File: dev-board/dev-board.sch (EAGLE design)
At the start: 37 parts, among them J1 12401832E402A, U1 STM32F103RET6, U2 AT24C64BN-10SU-2.7, U3 FT232RL, U4 MCP2551, U5 LM1117IMP-3.3, X1 8MHz

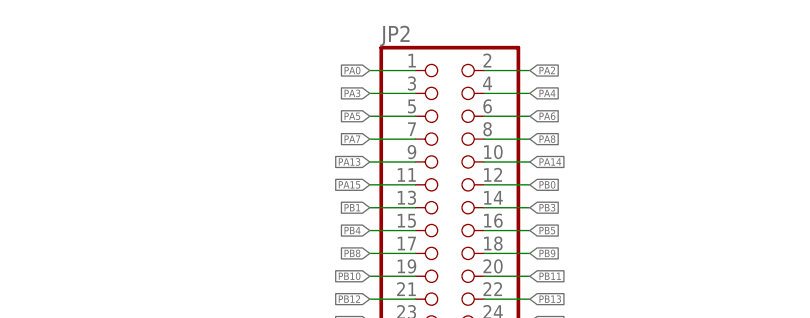
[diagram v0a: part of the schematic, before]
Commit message: Fix dev-board silkscreen
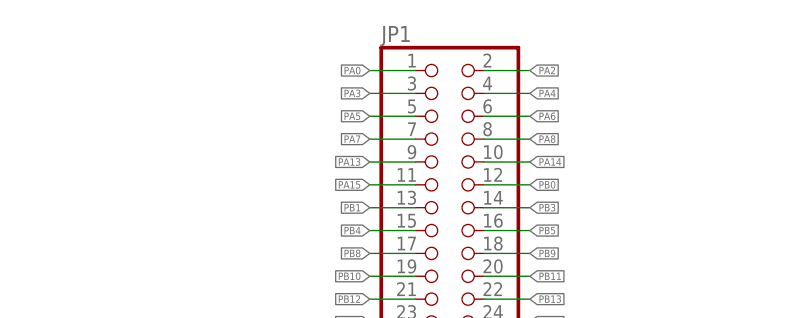
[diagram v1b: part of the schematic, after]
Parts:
- renumbered JP2 to JP1

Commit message: Fix some issues with the dev-board design
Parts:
- added JP2: PINHD-2X20, Connector:PINHD-2X20
- JP1: value PINHD-2X20 -> PINHD-1X4; device Connector:PINHD-2X20 -> Connector:PINHD-1X4
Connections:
- removed net PA13: JP1.9, U1A.PA13
- removed net PA14: JP1.10, U1A.PA14
- new net SWCLK: JP1.3, JP2.10, U1A.PA14
- new net SWDIO: JP1.2, JP2.9, U1A.PA13
- net +5V: now also JP1.1
- net GND: now also JP1.4
- net PA0: now also JP2.1; no longer JP1.1
- net PA15: now also JP2.11; no longer JP1.11
- net PA2: now also JP2.2; no longer JP1.2
- net PA3: now also JP2.3; no longer JP1.3
- net PA4: now also JP2.4; no longer JP1.4
- net PA5: now also JP2.5; no longer JP1.5
- net PA6: now also JP2.6; no longer JP1.6
- net PA7: now also JP2.7; no longer JP1.7
- net PA8: now also JP2.8; no longer JP1.8
- net PB0: now also JP2.12; no longer JP1.12
- net PB1: now also JP2.13; no longer JP1.13
- net PB10: now also JP2.19; no longer JP1.19
- net PB11: now also JP2.20; no longer JP1.20
- net PB12: now also JP2.21; no longer JP1.21
- net PB13: now also JP2.22; no longer JP1.22
- net PB14: now also JP2.23; no longer JP1.23
- net PB15: now also JP2.24; no longer JP1.24
- net PB3: now also JP2.14; no longer JP1.14
- net PB4: now also JP2.15; no longer JP1.15
- net PB5: now also JP2.16; no longer JP1.16
- net PB8: now also JP2.17; no longer JP1.17
- net PB9: now also JP2.18; no longer JP1.18
- net PC0: now also JP2.25; no longer JP1.25
- net PC1: now also JP2.26; no longer JP1.26
- net PC10: now also JP2.35; no longer JP1.35
- net PC11: now also JP2.36; no longer JP1.36
- net PC12: now also JP2.37; no longer JP1.37
- net PC13: now also JP2.38; no longer JP1.38
- net PC14: now also JP2.39; no longer JP1.39
- net PC15: now also JP2.40; no longer JP1.40
- net PC2: now also JP2.27; no longer JP1.27
- net PC3: now also JP2.28; no longer JP1.28
- net PC4: now also JP2.29; no longer JP1.29
- net PC5: now also JP2.30; no longer JP1.30
- net PC6: now also JP2.31; no longer JP1.31
- net PC7: now also JP2.32; no longer JP1.32
- net PC8: now also JP2.33; no longer JP1.33
- net PC9: now also JP2.34; no longer JP1.34

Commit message: Clean up dev-board schematic
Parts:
- R1, R11, R13, R14, R2, R3, R4, R7, R8: value 6K8 -> 10K
- R5, R6: value 6K8 -> 4k7
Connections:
- net N$14 renamed USBDP
- net N$16 renamed USBDM
- net N$7 renamed CANH
- net N$8 renamed CANL
- net +3V3: now also C3.1, U5.OUT_2; no longer C3.2
- net GND: now also C3.2, J1.SHIELD1, J1.SHIELD2, J1.SHIELD3, J1.SHIELD4; no longer C3.1
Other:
- moved on the sheet: C1, C10, C11, C12, C2, C3, C6, C7, J1, J2, R1, R10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

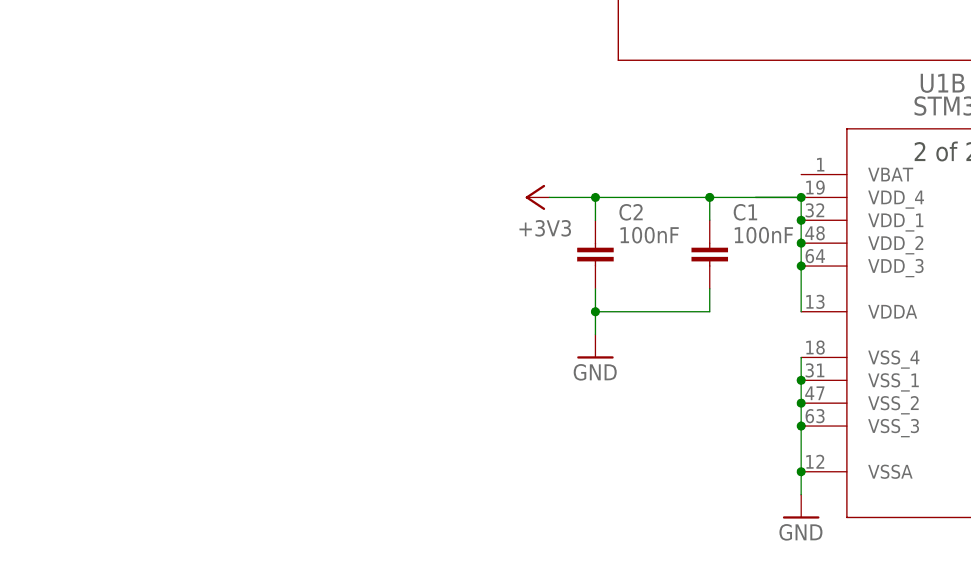
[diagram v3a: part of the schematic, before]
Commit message: Proper decoupling caps for stm32
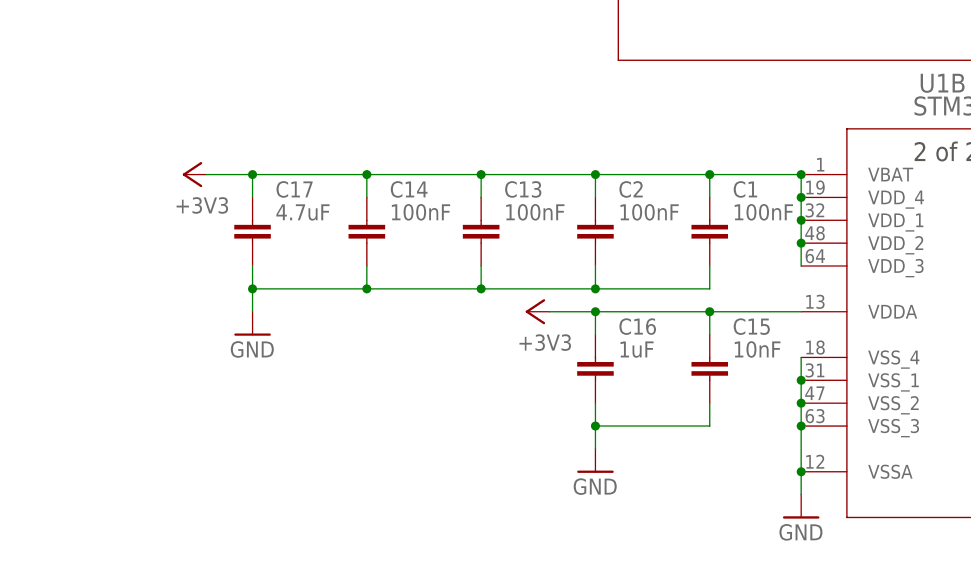
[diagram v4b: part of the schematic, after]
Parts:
- added C13, C14: 100nF, Capacitor:C_CHIP-0805(2012-METRIC)
- added C15: 10nF, Capacitor:C_CHIP-0805(2012-METRIC)
- added C16: 1uF, Capacitor:C_CHIP-0805(2012-METRIC)
- added C17: 4.7uF, Capacitor:C_CHIP-0805(2012-METRIC)
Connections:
- net +3V3: now also C13.1, C14.1, C15.1, C16.1, C17.1, U1B.VBAT
- net GND: now also C13.2, C14.2, C15.2, C16.2, C17.2
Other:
- moved on the sheet: C1, C2

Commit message: Proper bulk cap for regulator
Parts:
- C12: value 100nF -> 10uF
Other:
- moved on the sheet: C10, C11, C12, C3, C6, C7, C8, C9, J1, J2, R1, R10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

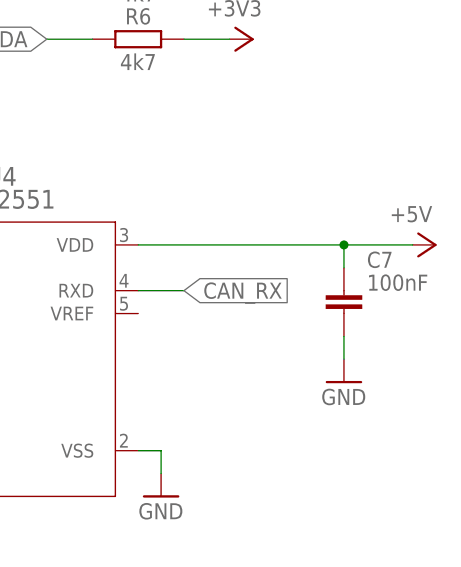
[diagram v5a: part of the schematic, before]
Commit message: Bulkier MCP2551 decoupling cap
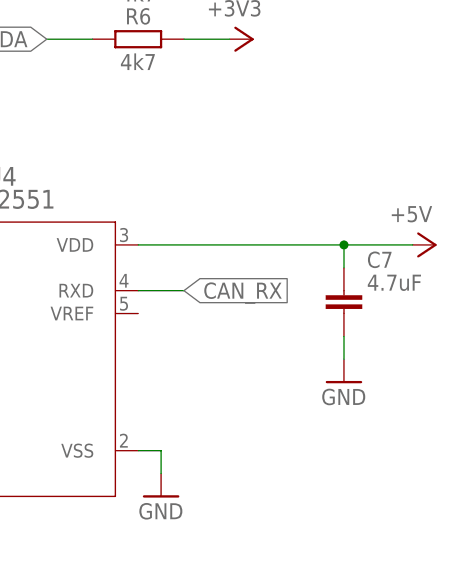
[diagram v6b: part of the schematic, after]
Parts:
- C7: value 100nF -> 4.7uF
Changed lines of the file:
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@@
 <part name="U4" library="IC_Interface" library_urn="urn:adsk.eagle:library:16378299" deviceset="MCP2551" device="_SOIC" package3d_urn="urn:adsk.eagle:package:16378326/2" value="MCP2551"/>
 <part name="GND11" library="supply1" library_urn="urn:adsk.eagle:library:371" deviceset="GND" device=""/>
-<part name="C7" library="Capacitor" library_urn="urn:adsk.eagle:library:16290819" deviceset="C" device="CHIP-0805(2012-METRIC)" package3d_urn="urn:adsk.eagle:package:16290897/2" technology="_" value="100nF"/>
+<part name="C7" library="Capacitor" library_urn="urn:adsk.eagle:library:16290819" deviceset="C" device="CHIP-0805(2012-METRIC)" package3d_urn="urn:adsk.eagle:package:16290897/2" technology="_" value="4.7uF"/>
 <part name="P+4" library="supply1" library_urn="urn:adsk.eagle:library:371" deviceset="+5V" device=""/>
 <part name="C8" library="Capacitor" library_urn="urn:adsk.eagle:library:16290819" deviceset="C" device="CHIP-0805(2012-METRIC)" package3d_urn="urn:adsk.eagle:package:16290897/2" technology="_" value="100nF"/>

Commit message: Fix stm32 decoupling caps in dev-board pcb design
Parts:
- added C18: 100nF, Capacitor:C_CHIP-0805(2012-METRIC)
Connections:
- net +3V3: now also C18.1
- net GND: now also C18.2
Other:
- moved on the sheet: C17
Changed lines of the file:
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@@
 <part name="GND28" library="supply1" library_urn="urn:adsk.eagle:library:371" deviceset="GND" device=""/>
 <part name="GND12" library="supply1" library_urn="urn:adsk.eagle:library:371" deviceset="GND" device=""/>
+<part name="C18" library="Capacitor" library_urn="urn:adsk.eagle:library:16290819" deviceset="C" device="CHIP-0805(2012-METRIC)" package3d_urn="urn:adsk.eagle:package:16290897/2" technology="_" value="100nF"/>
 </parts>
 <sheets>
@@
 <attribute name="VALUE" x="7.3406" y="-54.3814" size="2.0828" layer="96" ratio="6" rot="SR0"/>
 </instance>
-<instance part="+3V1" gate="G$1" x="-73.66" y="-60.96" smashed="yes" rot="R90">
-<attribute name="VALUE" x="-68.58" y="-63.5" size="1.778" layer="96" rot="R180"/>
+<instance part="+3V1" gate="G$1" x="-86.36" y="-60.96" smashed="yes" rot="R90">
+<attribute name="VALUE" x="-81.28" y="-63.5" size="1.778" layer="96" rot="R180"/>
 </instance>
 <instance part="C1" gate="G$1" x="-15.24" y="-66.04" smashed="yes">
@@
 <attribute name="VALUE" x="-30.48" y="-78.74" size="1.778" layer="96" rot="R180"/>
 </instance>
-<instance part="C17" gate="G$1" x="-66.04" y="-66.04" smashed="yes">
+<instance part="C17" gate="G$1" x="-78.74" y="-66.04" smashed="yes">
+<attribute name="NAME" x="-76.2" y="-63.5" size="1.778" layer="95"/>
+<attribute name="VALUE" x="-76.2" y="-66.04" size="1.778" layer="96"/>
+</instance>
+<instance part="GND28" gate="1" x="-78.74" y="-78.74" smashed="yes">
+<attribute name="VALUE" x="-81.28" y="-81.28" size="1.778" layer="96"/>
+</instance>
+<instance part="GND12" gate="1" x="86.36" y="-27.94" smashed="yes">
+<attribute name="VALUE" x="83.82" y="-30.48" size="1.778" layer="96"/>
+</instance>
+<instance part="C18" gate="G$1" x="-66.04" y="-66.04" smashed="yes">
 <attribute name="NAME" x="-63.5" y="-63.5" size="1.778" layer="95"/>
 <attribute name="VALUE" x="-63.5" y="-66.04" size="1.778" layer="96"/>
-</instance>
-<instance part="GND28" gate="1" x="-66.04" y="-78.74" smashed="yes">
-<attribute name="VALUE" x="-68.58" y="-81.28" size="1.778" layer="96"/>
-</instance>
-<instance part="GND12" gate="1" x="86.36" y="-27.94" smashed="yes">
-<attribute name="VALUE" x="83.82" y="-30.48" size="1.778" layer="96"/>
 </instance>
 </instances>
@@
 <wire x1="-15.24" y1="-63.5" x2="-15.24" y2="-60.96" width="0.1524" layer="91"/>
 <pinref part="+3V1" gate="G$1" pin="+3V3"/>
-<wire x1="-71.12" y1="-60.96" x2="-66.04" y2="-60.96" width="0.1524" layer="91"/>
+<wire x1="-83.82" y1="-60.96" x2="-78.74" y2="-60.96" width="0.1524" layer="91"/>
 <junction x="-27.94" y="-60.96"/>
 <pinref part="C14" gate="G$1" pin="1"/>
+<wire x1="-78.74" y1="-60.96" x2="-66.04" y2="-60.96" width="0.1524" layer="91"/>
 <wire x1="-66.04" y1="-60.96" x2="-53.34" y2="-60.96" width="0.1524" layer="91"/>
 <wire x1="-53.34" y1="-60.96" x2="-40.64" y2="-60.96" width="0.1524" layer="91"/>
@@
 <junction x="-40.64" y="-60.96"/>
 <pinref part="C17" gate="G$1" pin="1"/>
-<wire x1="-66.04" y1="-63.5" x2="-66.04" y2="-60.96" width="0.1524" layer="91"/>
-<junction x="-66.04" y="-60.96"/>
+<wire x1="-78.74" y1="-63.5" x2="-78.74" y2="-60.96" width="0.1524" layer="91"/>
+<junction x="-78.74" y="-60.96"/>
 <pinref part="U1" gate="B" pin="VBAT"/>
 <pinref part="U1" gate="B" pin="VDD_4"/>
@@
 <junction x="-15.24" y="-60.96"/>
 <junction x="-5.08" y="-60.96"/>
+<pinref part="C18" gate="G$1" pin="1"/>
+<wire x1="-66.04" y1="-63.5" x2="-66.04" y2="-60.96" width="0.1524" layer="91"/>
+<junction x="-66.04" y="-60.96"/>
 </segment>
 <segment>
@@
 </segment>
 <segment>
-<pinref part="C2" gate="G$1" pin="2"/>
-<wire x1="-27.94" y1="-71.12" x2="-27.94" y2="-73.66" width="0.1524" layer="91"/>
-<wire x1="-27.94" y1="-73.66" x2="-15.24" y2="-73.66" width="0.1524" layer="91"/>
-<pinref part="C1" gate="G$1" pin="2"/>
-<wire x1="-15.24" y1="-73.66" x2="-15.24" y2="-71.12" width="0.1524" layer="91"/>
-<junction x="-27.94" y="-73.66"/>
-<pinref part="C14" gate="G$1" pin="2"/>
-<wire x1="-53.34" y1="-71.12" x2="-53.34" y2="-73.66" width="0.1524" layer="91"/>
-<wire x1="-53.34" y1="-73.66" x2="-40.64" y2="-73.66" width="0.1524" layer="91"/>
-<pinref part="C13" gate="G$1" pin="2"/>
-<wire x1="-40.64" y1="-73.66" x2="-27.94" y2="-73.66" width="0.1524" layer="91"/>
-<wire x1="-40.64" y1="-71.12" x2="-40.64" y2="-73.66" width="0.1524" layer="91"/>
-<junction x="-40.64" y="-73.66"/>
-<junction x="-53.34" y="-73.66"/>
-<pinref part="C17" gate="G$1" pin="2"/>
-<wire x1="-66.04" y1="-71.12" x2="-66.04" y2="-73.66" width="0.1524" layer="91"/>
-<wire x1="-66.04" y1="-76.2" x2="-66.04" y2="-73.66" width="0.1524" layer="91"/>
-<wire x1="-53.34" y1="-73.66" x2="-66.04" y2="-73.66" width="0.1524" layer="91"/>
-<junction x="-66.04" y="-73.66"/>
-<pinref part="GND28" gate="1" pin="GND"/>
-</segment>
-<segment>
 <pinref part="U1" gate="B" pin="VSS_4"/>
 <pinref part="U1" gate="B" pin="VSS_1"/>
@@
 <pinref part="GND12" gate="1" pin="GND"/>
 </segment>
-</net>
+<segment>
+<pinref part="C2" gate="G$1" pin="2"/>
+<wire x1="-27.94" y1="-71.12" x2="-27.94" y2="-73.66" width="0.1524" layer="91"/>
+<wire x1="-27.94" y1="-73.66" x2="-15.24" y2="-73.66" width="0.1524" layer="91"/>
+<pinref part="C1" gate="G$1" pin="2"/>
+<wire x1="-15.24" y1="-73.66" x2="-15.24" y2="-71.12" width="0.1524" layer="91"/>
+<junction x="-27.94" y="-73.66"/>
+<pinref part="C14" gate="G$1" pin="2"/>
+<wire x1="-53.34" y1="-71.12" x2="-53.34" y2="-73.66" width="0.1524" layer="91"/>
+<wire x1="-53.34" y1="-73.66" x2="-40.64" y2="-73.66" width="0.1524" layer="91"/>
+<pinref part="C13" gate="G$1" pin="2"/>
+<wire x1="-40.64" y1="-73.66" x2="-27.94" y2="-73.66" width="0.1524" layer="91"/>
+<wire x1="-40.64" y1="-71.12" x2="-40.64" y2="-73.66" width="0.1524" layer="91"/>
+<junction x="-40.64" y="-73.66"/>
+<junction x="-53.34" y="-73.66"/>
+<wire x1="-53.34" y1="-73.66" x2="-66.04" y2="-73.66" width="0.1524" layer="91"/>
+<pinref part="C18" gate="G$1" pin="2"/>
+<wire x1="-66.04" y1="-73.66" x2="-66.04" y2="-71.12" width="0.1524" layer="91"/>
+<pinref part="C17" gate="G$1" pin="2"/>
+<wire x1="-78.74" y1="-71.12" x2="-78.74" y2="-73.66" width="0.1524" layer="91"/>
+<wire x1="-78.74" y1="-73.66" x2="-66.04" y2="-73.66" width="0.1524" layer="91"/>
+<junction x="-66.04" y="-73.66"/>
+<wire x1="-78.74" y1="-73.66" x2="-78.74" y2="-76.2" width="0.1524" layer="91"/>
+<junction x="-78.74" y="-73.66"/>
+<pinref part="GND28" gate="1" pin="GND"/>
+</segment>
+</net>

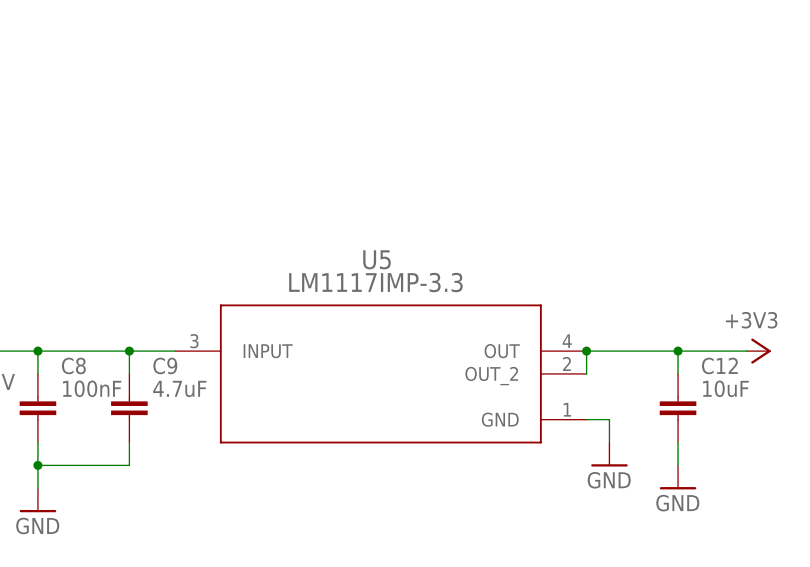
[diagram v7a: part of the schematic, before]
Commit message: Remove designator labels around regulator in dev-boarc pcb
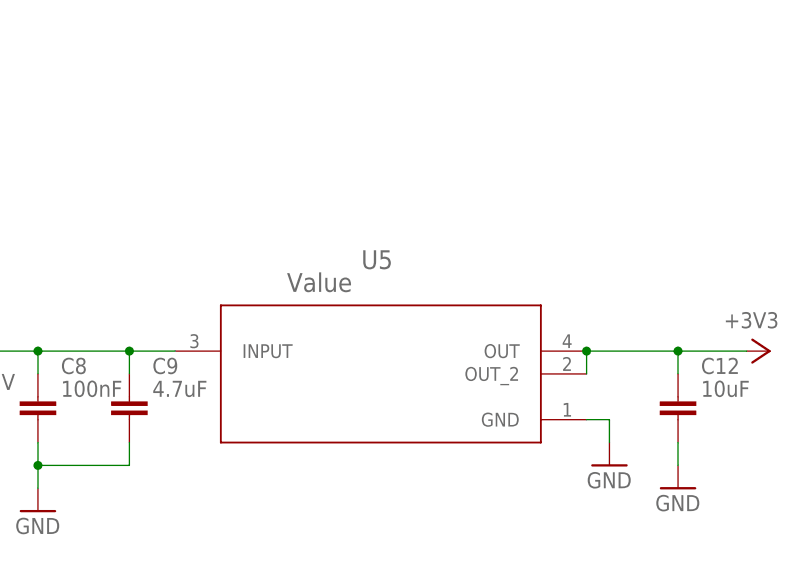
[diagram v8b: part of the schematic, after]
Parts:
- U5: value LM1117IMP-3.3 -> Value
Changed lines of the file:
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@@
 <part name="GND16" library="supply1" library_urn="urn:adsk.eagle:library:371" deviceset="GND" device=""/>
 <part name="+3V6" library="supply1" library_urn="urn:adsk.eagle:library:371" deviceset="+3V3" device=""/>
-<part name="U5" library="LM1117IMP-3.3" deviceset="LM1117IMP-3.3/NOPB" device="" value="LM1117IMP-3.3"/>
+<part name="U5" library="LM1117IMP-3.3" deviceset="LM1117IMP-3.3/NOPB" device="" value="Value"/>
 <part name="C12" library="Capacitor" library_urn="urn:adsk.eagle:library:16290819" deviceset="C" device="CHIP-0805(2012-METRIC)" package3d_urn="urn:adsk.eagle:package:16290897/2" technology="_" value="10uF"/>
 <part name="JP2" library="Connector" library_urn="urn:adsk.eagle:library:16378166" deviceset="PINHD-2X20" device="" package3d_urn="urn:adsk.eagle:package:22443/2"/>
